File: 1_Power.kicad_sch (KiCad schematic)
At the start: 35 parts, among them Q201 IRLZ44N, Q202 IRLZ44N, U201 BQ24005, U202 LM74700, U203 LM74700, U204 NCP1117-3.3, U205 LMR51430, U206 TPS7A2033PDBVR

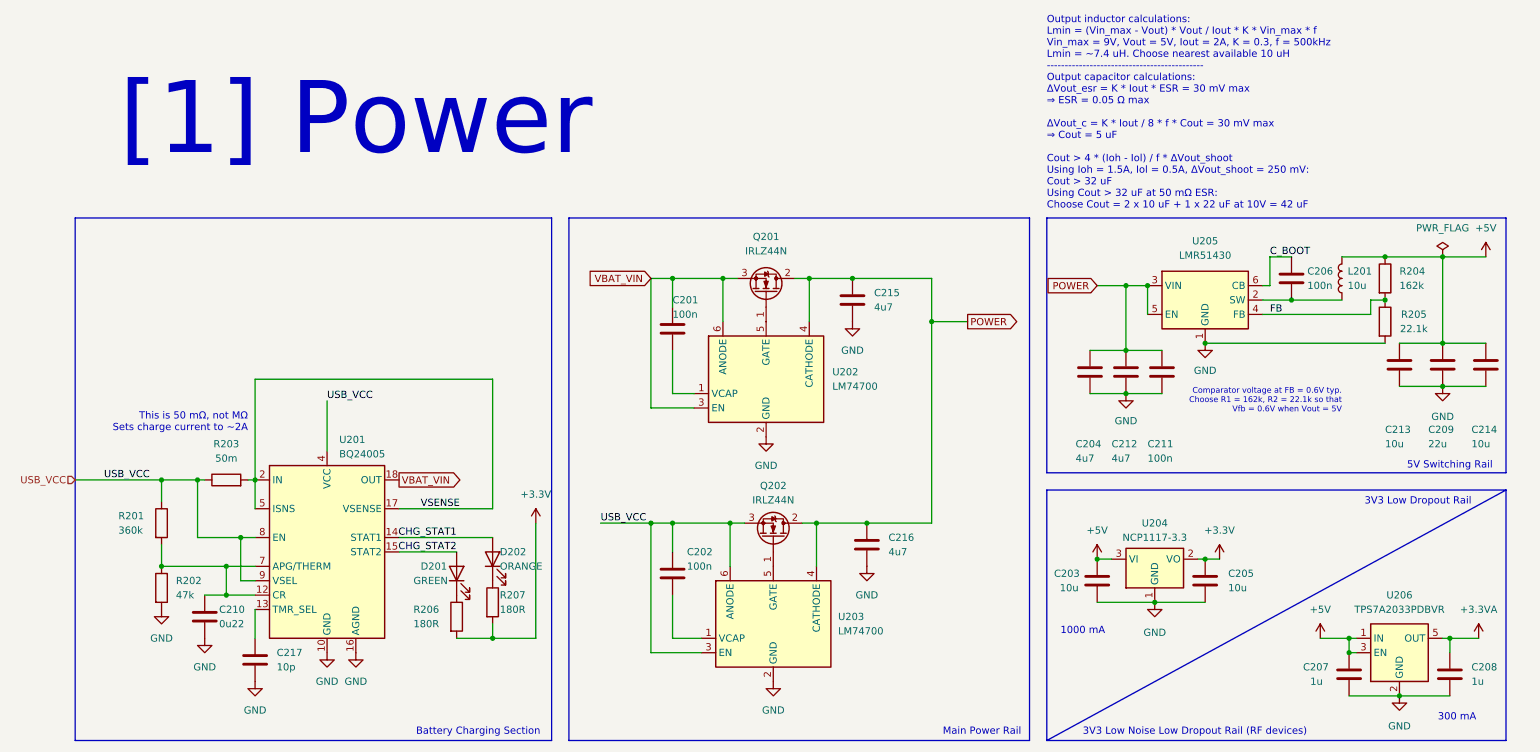
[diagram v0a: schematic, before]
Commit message: Corrected power section for the billionth time Added programming notes
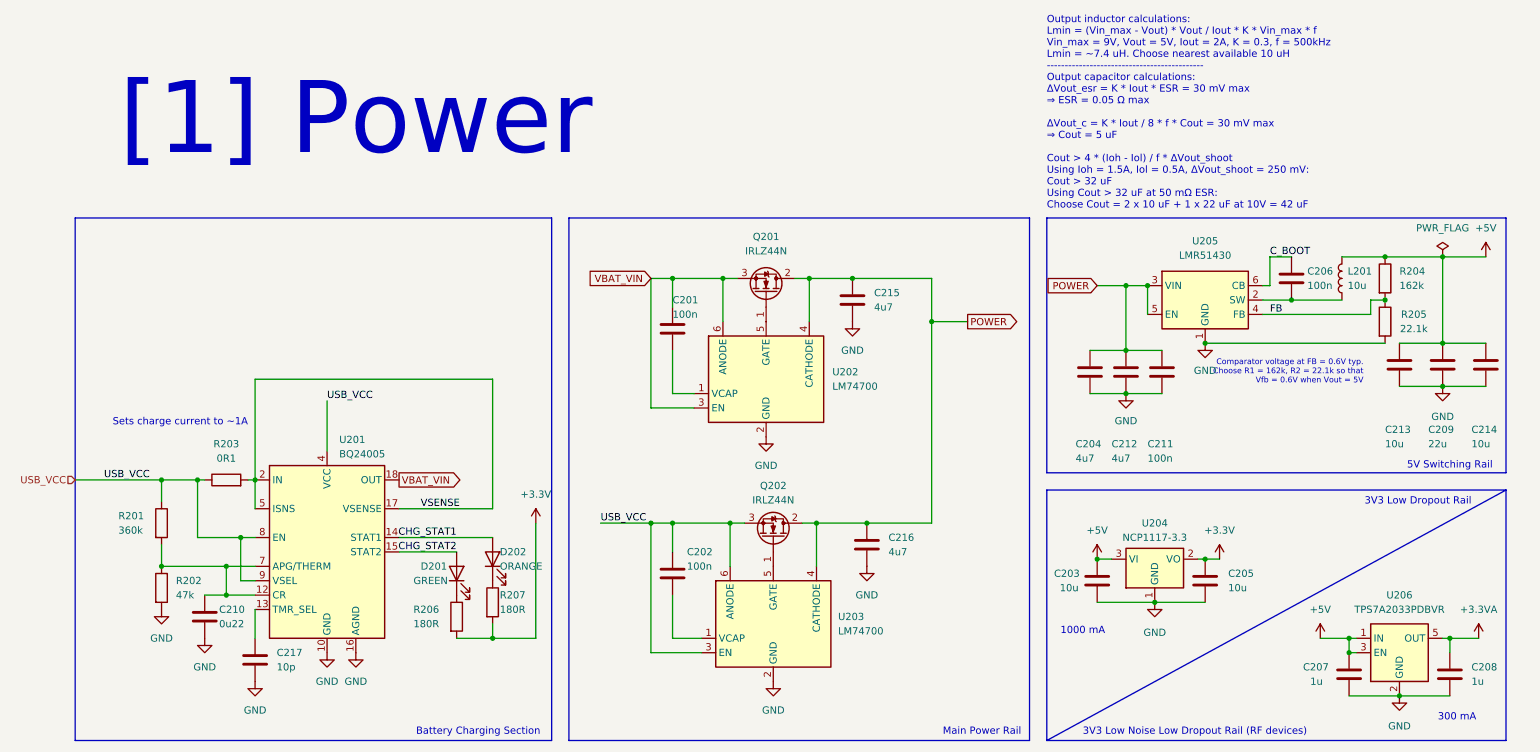
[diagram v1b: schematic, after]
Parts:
- R203: value 50m -> 0R1
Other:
- note added: "Sets charge current to ~1A"
- note removed: "This is 50 mΩ, not MΩ Sets charge current to ~2A"
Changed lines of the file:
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@@
 	(text "Comparator voltage at FB = 0.6V typ.\nChoose R1 = 162k, R2 = 22.1k so that\nVfb = 0.6V when Vout = 5V"
 		(exclude_from_sim no)
-		(at 245.11 88.9 0)
-		(effects
-			(font
-				(size 1.016 1.016)
+		(at 248.92 83.82 0)
+		(effects
+			(font
+				(face "Arial")
+				(size 1 1)
 			)
 			(justify right)
@@
 		)
 	)
-	(text "This is 50 mΩ, not MΩ\nSets charge current to ~2A"
+	(text "Sets charge current to ~1A"
 		(exclude_from_sim no)
 		(at 52.07 92.71 0)
@@
 			)
 		)
-		(property "Value" "50m"
+		(property "Value" "0R1"
 			(at 48.26 99.06 90)
 			(show_name no)

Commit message: Added Title Block
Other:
- title: (none) -> Polaris/Power
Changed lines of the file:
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@@
 	(generator_version "10.0")
 	(paper "A4")
+	(title_block
+		(title "Polaris/Power")
+	)
 	(rectangle
 		(start 108.712 56.642)

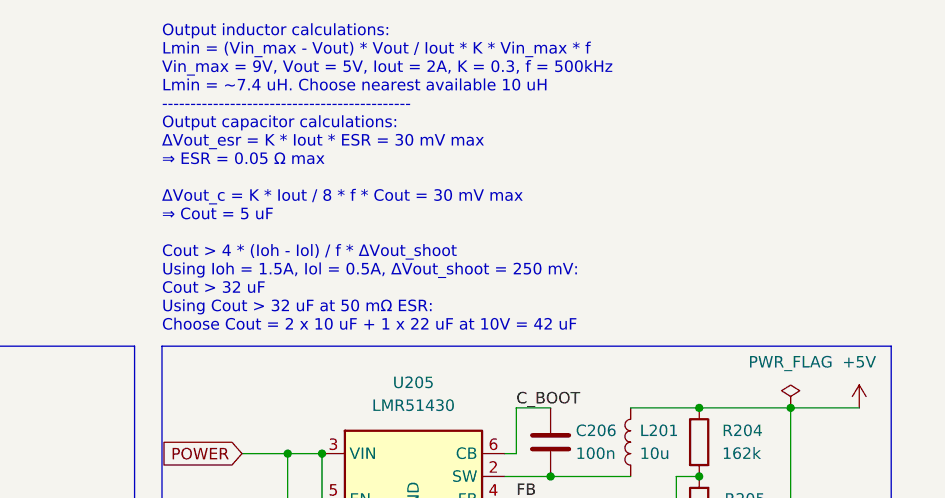
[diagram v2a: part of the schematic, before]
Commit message: Added more notes and finished footprint assignment
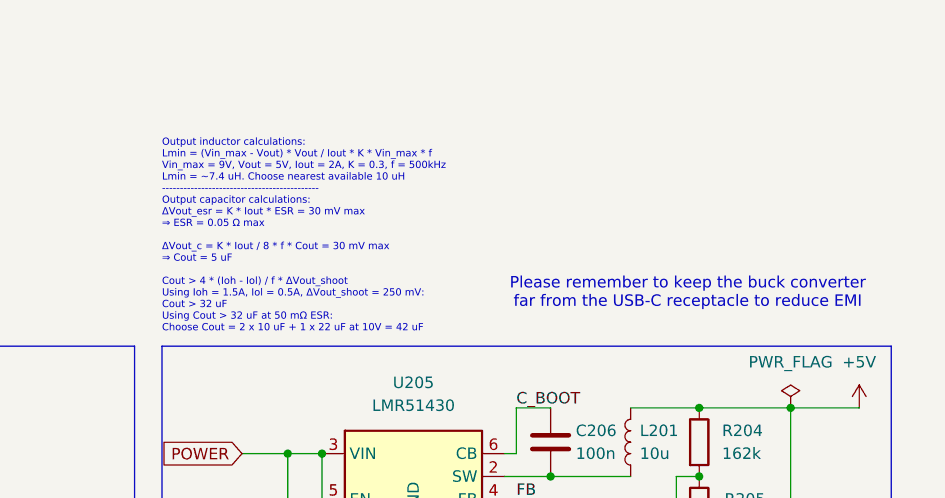
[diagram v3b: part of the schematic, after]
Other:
- note added: "Please remember to keep the buck converter far from the USB-C receptacle to reduce EMI"

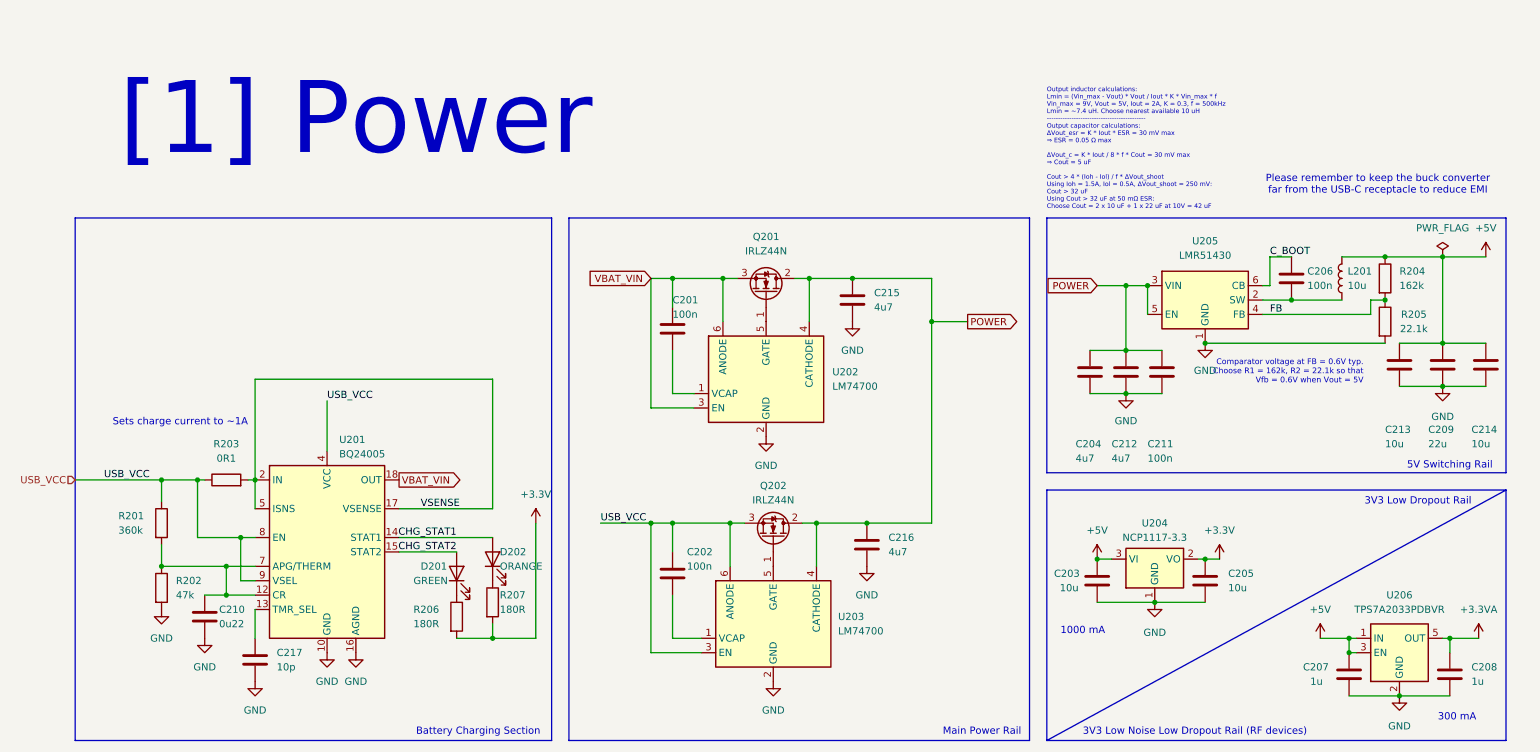
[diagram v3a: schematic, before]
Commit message: Finally started the PCB layout and routing Only took me a few decades Also labeled some unlabeled nets in the schematic Changed the USB mux to be two 1x3 pin headers instead of one 2x3 Edited symbols and footprints to match pin numbers
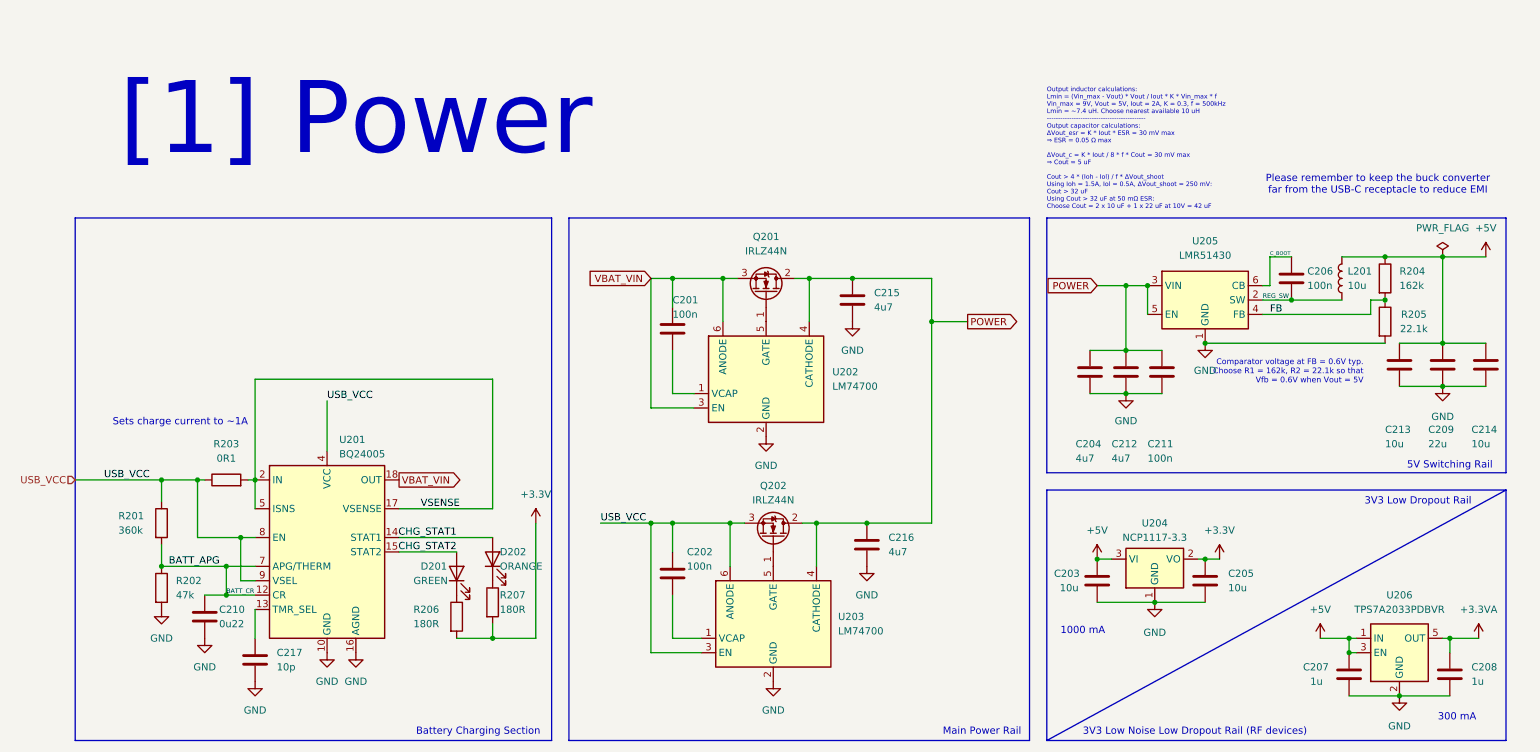
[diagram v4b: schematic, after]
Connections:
- net REG_SW: now reaches C206.2, L201.1, U205.2 (SW)
- net BATT_APG: now reaches C210.1, R201.2, R202.1, U201.12 (CR), U201.7 (APG/THERM)
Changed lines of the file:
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@@
 		(effects
 			(font
-				(size 1.27 1.27)
+				(size 0.65 0.65)
 			)
 			(justify left bottom)
@@
 			)
 			(justify left bottom)
+		)
+	)
+	(label "BATT_APG"
+		(at 38.1 118.11 0)
+		(effects
+			(font
+				(size 1.27 1.27)
+			)
+			(justify left bottom)
+		)
+	)
+	(label "BATT_CR"
+		(at 48.26 123.19 0)
+		(effects
+			(font
+				(size 0.8 0.8)
+			)
+			(justify left bottom)
+		)
+	)
+	(label "REG_SW"
+		(at 231.14 71.12 0)
+		(effects
+			(font
+				(size 0.8 0.8)
+			)
+			(justify left bottom)

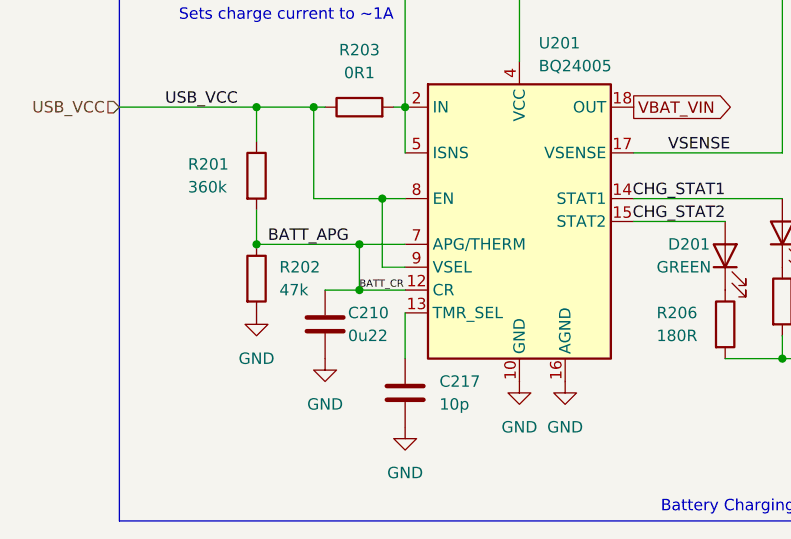
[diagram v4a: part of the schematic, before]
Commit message: Renamed a few nets
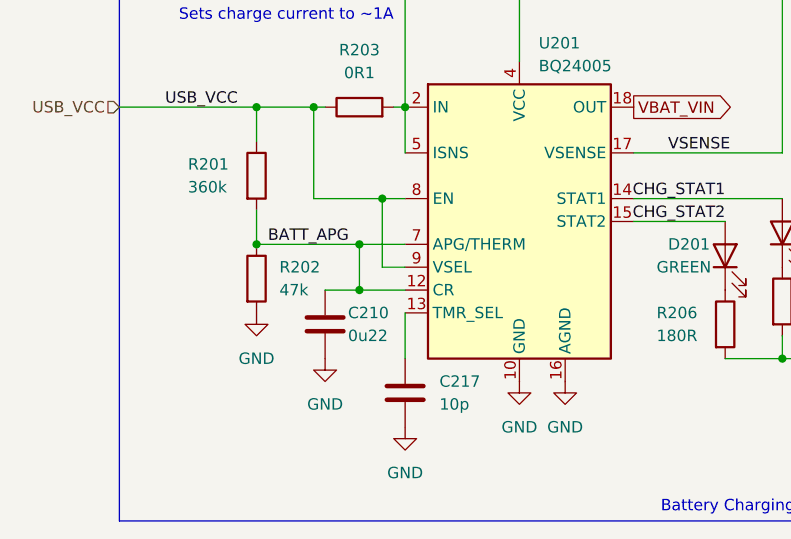
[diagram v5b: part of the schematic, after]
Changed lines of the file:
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@@
-		)
-	)
-	(label "BATT_CR"
-		(at 48.26 123.19 0)
-		(effects
-			(font
-				(size 0.8 0.8)
-			)
-			(justify left bottom)
 		)
 	)

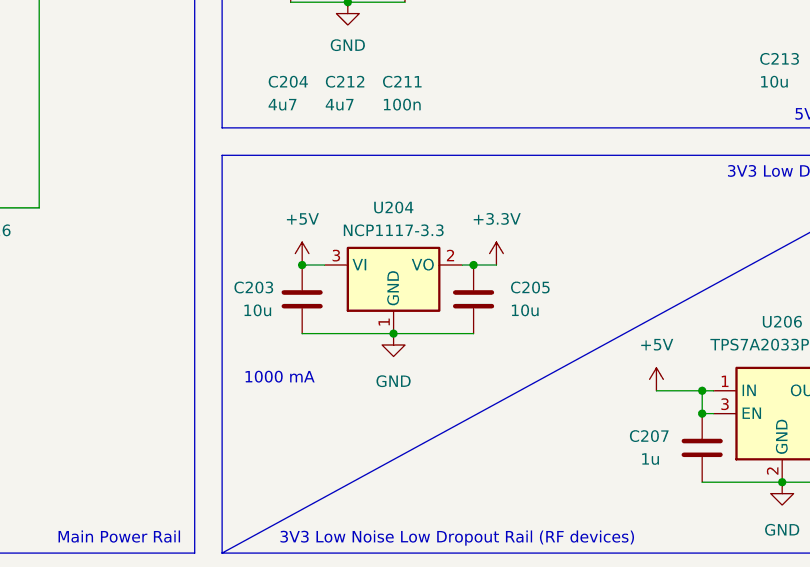
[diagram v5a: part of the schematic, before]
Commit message: Switched main 3.3V LDO to a modern part
New one: TLV75733
Old one: NCP1117
New one has cleaner output, lower dropout voltage and is cheaper.

Also continued completing the connections for NAV
Updated README to include changes to architecture
Also updated pin connections on CubeMX (ioc) file
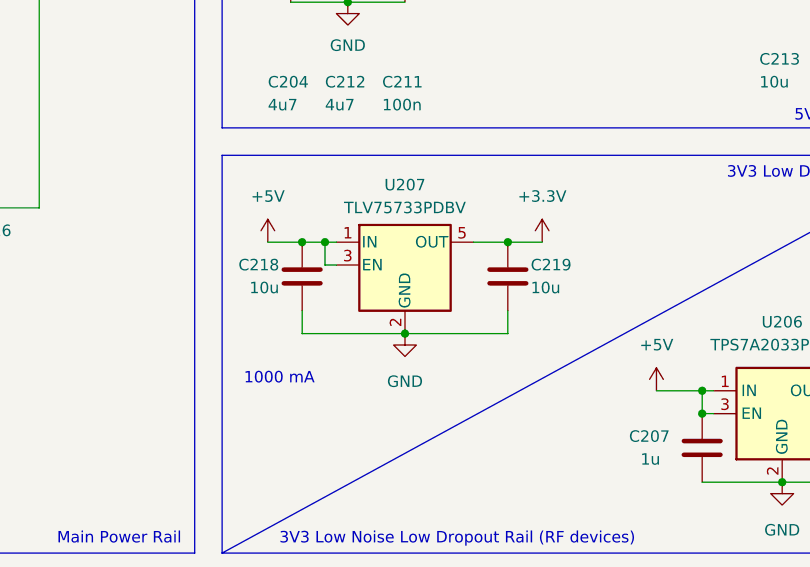
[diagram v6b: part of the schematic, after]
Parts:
- removed C203, C205: 10u, Capacitor_SMD:C_0805_2012Metric, symbol Device:C
- removed U204: NCP1117-3.3, Package_TO_SOT_SMD:SOT-223-3_TabPin2, symbol Regulator_Linear:NCP1117-3.3_SOT223
- added C218, C219: 10u, Capacitor_SMD:C_0805_2012Metric, symbol Device:C
- added U207: TLV75733PDBV, Package_TO_SOT_SMD:SOT-23-5, symbol Regulator_Linear:TLV75733PDBV
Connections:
- net +3.3V: now also C219.1, U207.5 (OUT)
- net +5V: now also C218.1, U207.1 (IN), U207.3 (EN)
- net GND: now also C218.2, C219.2, U207.2 (GND)
